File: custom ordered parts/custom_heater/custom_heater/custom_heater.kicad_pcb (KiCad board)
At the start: 2 copper layers, 119 x 119 mm, 2 parts

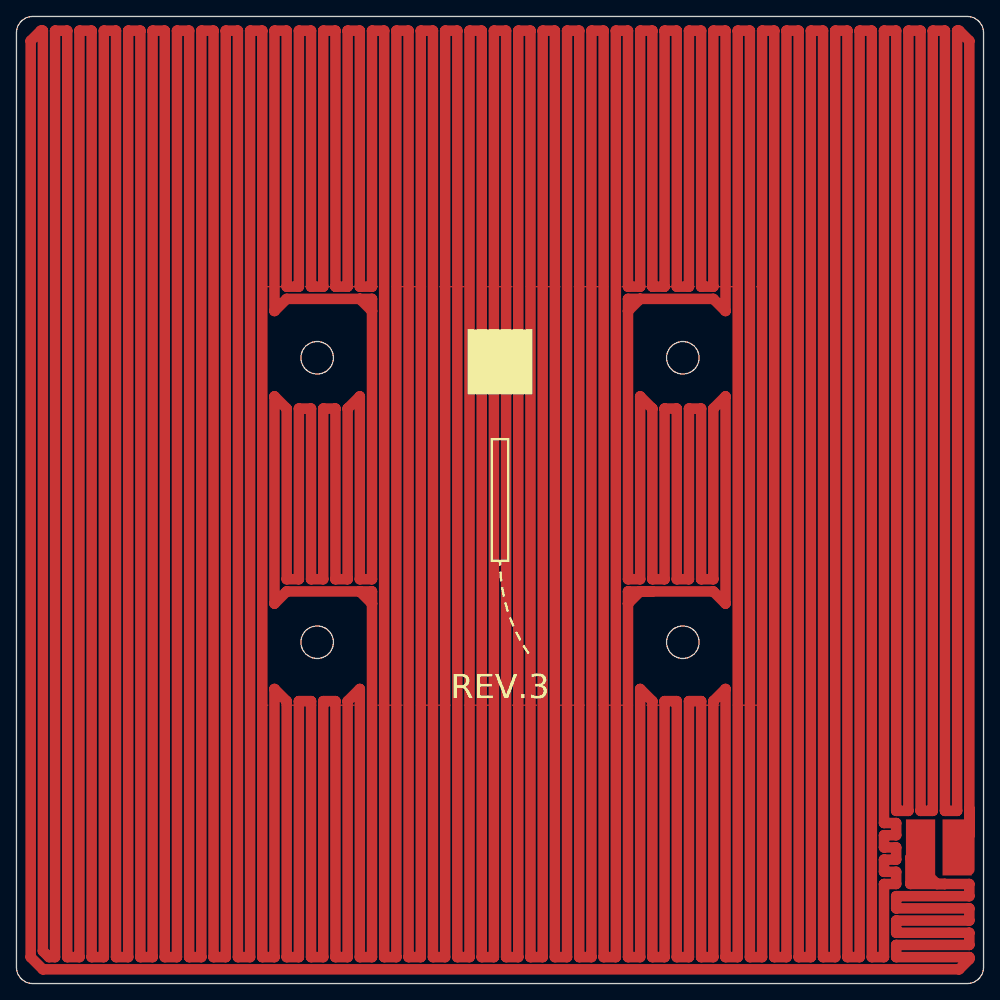
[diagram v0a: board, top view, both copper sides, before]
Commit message: Use SMT thermistor on the bed which is more reliable and cheaper
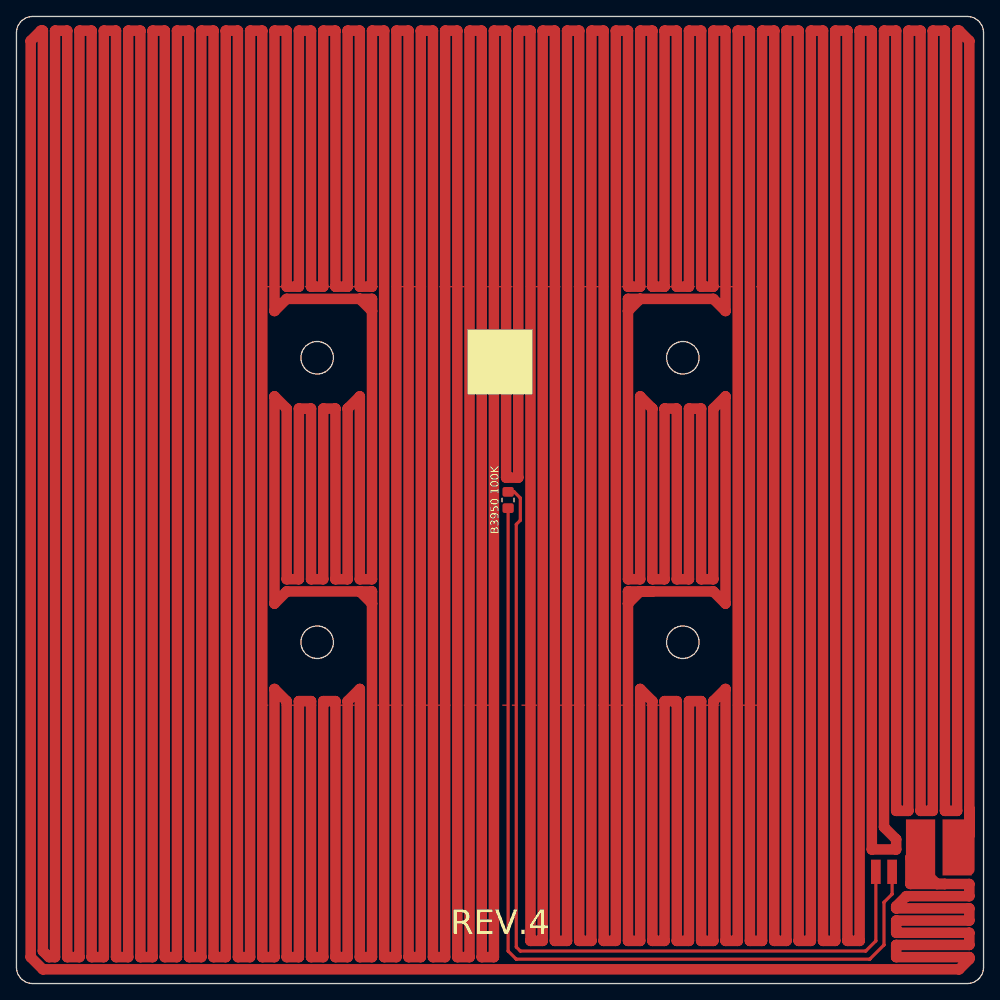
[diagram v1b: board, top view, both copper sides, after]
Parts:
- added ?: , , F.Cu at (199.7, 145.8)
- added ?: , , F.Cu at (201.7, 145.8)
- added B3950 100K: R_0805_2012Metric_Pad1.20x1.40mm_HandSolder, Resistor_SMD:R_0805_2012Metric_Pad1.20x1.40mm_HandSolder, F.Cu at (154.4, 100.1)
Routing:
- net (no net): track 8752.5 -> 8766.7 mm
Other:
- board text added: "REV.4"
- board text removed: "REV.3"
